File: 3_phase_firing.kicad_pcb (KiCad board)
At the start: 2 copper layers, 142.5 x 77.5 mm, 66 parts, among them J1 IN1, J2 IN2, J3 OUT, J4 USB_LED, J5 POWER, Q1 MMBT3904, Q2 MMBT3904, Q3 MMBT3904, U1 LM339, U10 4N35, U11 4N35, U12 4N35, U2 L7812, U3 4N35, U4 4N35, U5 4N35, U6 YAAJ_WeAct_BlackPill_Part_Like, U7 4N35, U8 4N35, U9 4N35

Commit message: fixing schematics and pcb layout, adding usb and knob control
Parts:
- removed G***: LOGO, logo_uny:logo_uny_15mm
- removed R28, R29: 220, Resistor_SMD:R_0805_2012Metric
- removed REF** (x3): MountingHole_3.2mm_M3_DIN965_Pad, MountingHole:MountingHole_3.2mm_M3_DIN965_Pad
- added J6: Conn_01x02, Connector_JST:JST_XH_B2B-XH-A_1x02_P2.50mm_Vertical, F.Cu at (167.6, 48.3)
- added J7: Conn_01x03, Connector_JST:JST_XH_B3B-XH-A_1x03_P2.50mm_Vertical, F.Cu at (132.1, 48.3)
- added J8: Conn_01x02, Connector_JST:JST_XH_B2B-XH-A_1x02_P2.50mm_Vertical, F.Cu at (157.5, 48.3)
- added Q4: MMBT3904, Package_TO_SOT_SMD:SOT-23, F.Cu at (162.6, 86.4)
- added Q5: MMBT3904, Package_TO_SOT_SMD:SOT-23, F.Cu at (164.2, 71.1)
- added Q6: MMBT3904, Package_TO_SOT_SMD:SOT-23, F.Cu at (162.6, 104.1)
- added kibuzzard-63D55C26: G***, kibuzzard-63D55C26, F.Cu at (77.9, 63.1)
- J4: value USB_LED -> USB_B; footprint Connector_JST:JST_XH_B2B-XH-A_1x02_P2.50mm_Vertical -> Connector_USB:USB_B_OST_USB-B1HSxx_Horizontal
- J5: value POWER -> Conn_01x03; footprint Connector_JST:JST_XH_B2B-XH-A_1x02_P2.50mm_Vertical -> Connector_JST:JST_XH_B3B-XH-A_1x03_P2.50mm_Vertical
- moved J3 114.8 mm to (128.3, 27.7), turned to 0 degrees
- moved J5 75.0 mm to (144.8, 48.3)
- moved D5 18.4 mm to (100.1, 68.1)
- moved C1 8.26 mm to (90.8, 59.6), turned to 180 degrees
- moved J4 4.77 mm to (167.6, 110.3), turned to -90 degrees
- moved R4 1.31 mm to (98.6, 93.4), turned to 90 degrees
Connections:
- net Net-(C1-Pad1) renamed /DB_D_OUT
- D1 pad 1: GNDS -> /DB_OUT
- D1 pad 2: PHASE_A -> GNDS
- D1 pad 3: Net-(D1-Pad3) -> NEUT
- D1 pad 4: NEUT -> PHASE_A
- D5 pad 2: Net-(D1-Pad3) -> /DB_OUT
- J4 pad 1: Net-(J4-Pad1) -> unconnected-(J4-Pad1)
- J4 pad 2: GND -> unconnected-(J4-Pad2)
- J5 pad 1: Net-(J5-Pad1) -> +3.3V
- J5 pad 2: GND -> ANGLE_CONTROL
- U6 pad 2: LED_USB -> LED_INDICATOR_2
- U6 pad 22: unconnected-(U6-Pad22) -> LED_INDICATOR_1
- U6 pad 26: ZCD_A -> ANGLE_CONTROL
- U6 pad 27: GATE_A1 -> unconnected-(U6-Pad27)
- U6 pad 28: GATE_A2 -> unconnected-(U6-Pad28)
- U6 pad 3: unconnected-(U6-Pad3) -> TRIAC_MODE
- U6 pad 31: unconnected-(U6-Pad31) -> ZCD_A
- U6 pad 4: TRIAC_MODE -> SCR_MODE
- U6 pad 7: unconnected-(U6-Pad7) -> GATE_A2
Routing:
- net TRIAC_MODE: track 110.2 -> 0.00 mm, vias 6 -> 0
- net ZCD_A: track 81.9 -> 0.00 mm, vias 2 -> 0
- net ZCD_B: track 79.7 -> 0.00 mm, vias 2 -> 0
- net LED_USB: track 74.1 -> 0.00 mm, vias 1 -> 0
- net GNDS: track 85.3 -> 16.1 mm, vias 22 -> 37
- net GATE_C1: track 54.0 -> 0.00 mm, vias 1 -> 0
- net GATE_C2: track 46.3 -> 0.00 mm
- net GATE_A1: track 35.2 -> 0.00 mm
- net PHASE_A: track 33.3 -> 0.00 mm
- net OUTC2_C: track 30.9 -> 0.00 mm, vias 1 -> 0
- net OUTB2_C: track 30.6 -> 0.00 mm, vias 1 -> 0
- net OUTA2_C: track 30.4 -> 0.00 mm, vias 1 -> 0
- net OUTC2_E: track 29.4 -> 0.00 mm
- net GATE_A2: track 28.7 -> 0.00 mm, vias 2 -> 0
- net OUTB2_E: track 25.2 -> 0.00 mm
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- added copper zone on F.Cu, net /DB_D_OUT
- added copper zone on F.Cu, net /DB_OUT
- added copper zone on F.Cu, net GNDS
- added copper zone on F.Cu, net NEUT
- added copper zone on F.Cu, net Net-(R5-Pad1)
- added copper zone on F.Cu, net PHASE_A
- added copper zone on F.Cu, net PHASE_B
- added copper zone on F.Cu, net PHASE_C
- added copper zone on B.Cu, net VCC
- removed copper zone on F.Cu, net +3.3V
- removed copper zone on B.Cu, net GND
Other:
- board text added: "HW-ID : ACRC-01 REV NUM : v0.3"
- board text removed: "!!!HIGH VOLTAGE!!!"
- board text removed: "HW-ID : ACRC-01 REV NUM : v0.2"
- board text removed: "N"

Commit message: done with all revision
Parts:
- removed D11: 1N4007, Diode_SMD:D_SMA_Handsoldering
- removed Q4, Q5, Q6: MMBT3904, Package_TO_SOT_SMD:SOT-23
- added R28: 1K, Resistor_SMD:R_1206_3216Metric_Pad1.30x1.75mm_HandSolder, F.Cu at (186.6, 69.1)
- added R29: 1K, Resistor_SMD:R_1206_3216Metric_Pad1.30x1.75mm_HandSolder, F.Cu at (186.6, 66.6)
- added R30: 1K, Resistor_SMD:R_1206_3216Metric_Pad1.30x1.75mm_HandSolder, B.Cu at (186.6, 69.1)
- added R31: 1K, Resistor_SMD:R_1206_3216Metric_Pad1.30x1.75mm_HandSolder, B.Cu at (186.6, 66.6)
- added R32: 1K, Resistor_SMD:R_1206_3216Metric_Pad1.30x1.75mm_HandSolder, F.Cu at (186.6, 83.7)
- added R33: 1K, Resistor_SMD:R_1206_3216Metric_Pad1.30x1.75mm_HandSolder, F.Cu at (186.6, 86.2)
- added R34: 1K, Resistor_SMD:R_1206_3216Metric_Pad1.30x1.75mm_HandSolder, B.Cu at (186.6, 83.7)
- added R35: 1K, Resistor_SMD:R_1206_3216Metric_Pad1.30x1.75mm_HandSolder, B.Cu at (186.6, 86.2)
- added R36: 1K, Resistor_SMD:R_1206_3216Metric_Pad1.30x1.75mm_HandSolder, F.Cu at (186.6, 100.9)
- added R37: 1K, Resistor_SMD:R_1206_3216Metric_Pad1.30x1.75mm_HandSolder, F.Cu at (186.6, 103.4)
- added R38: 1K, Resistor_SMD:R_1206_3216Metric_Pad1.30x1.75mm_HandSolder, B.Cu at (186.6, 100.9)
- added R39: 1K, Resistor_SMD:R_1206_3216Metric_Pad1.30x1.75mm_HandSolder, B.Cu at (186.6, 103.4)
- added R40: 220, Resistor_SMD:R_1206_3216Metric_Pad1.30x1.75mm_HandSolder, F.Cu at (132.1, 55.4)
- added R41: 10K, Resistor_SMD:R_0805_2012Metric, F.Cu at (168.8, 55.5)
- added R42: 10K, Resistor_SMD:R_0805_2012Metric, F.Cu at (153.0, 52.8)
- added REF**: MountingHole_3.2mm_M3, MountingHole:MountingHole_3.2mm_M3, F.Cu at (177.5, 116.2)
- added REF**: MountingHole_3.2mm_M3, MountingHole:MountingHole_3.2mm_M3, F.Cu at (80.1, 54.8)
- added REF**: MountingHole_3.2mm_M3, MountingHole:MountingHole_3.2mm_M3, F.Cu at (152.6, 116.2)
- added REF**: MountingHole_3.2mm_M3, MountingHole:MountingHole_3.2mm_M3, F.Cu at (200.1, 46.5)
- added REF**: MountingHole_3.2mm_M3, MountingHole:MountingHole_3.2mm_M3, F.Cu at (110.1, 101.8)
- added REF**: MountingHole_3.2mm_M3, MountingHole:MountingHole_3.2mm_M3, F.Cu at (200.1, 115.8)
- added kibuzzard-63D8BD9F: G***, kibuzzard-63D8BD9F, F.Cu at (154.6, 111.7)
- added kibuzzard-63DA9566: G***, kibuzzard-63DA9566, F.Cu at (207.2, 58.4)
- added kibuzzard-63DA9566: G***, kibuzzard-63DA9566, F.Cu at (207.1, 99.1)
- added kibuzzard-63DA95C1: G***, kibuzzard-63DA95C1, F.Cu at (192.6, 68.5)
- added kibuzzard-63DA9616: G***, kibuzzard-63DA9616, F.Cu at (192.6, 109.5)
- added kibuzzard-63DA961C: G***, kibuzzard-63DA961C, F.Cu at (192.6, 89.2)
- added kibuzzard-63DA96B7: G***, kibuzzard-63DA96B7, F.Cu at (207.2, 68.6)
- added kibuzzard-63DA96B7: G***, kibuzzard-63DA96B7, F.Cu at (207.1, 109.2)
- added kibuzzard-63DA974B: G***, kibuzzard-63DA974B, F.Cu at (207.2, 63.5)
- added kibuzzard-63DA974B: G***, kibuzzard-63DA974B, F.Cu at (207.1, 104.2)
- added kibuzzard-63DA9751: G***, kibuzzard-63DA9751, F.Cu at (207.2, 53.5)
- added kibuzzard-63DA9751: G***, kibuzzard-63DA9751, F.Cu at (207.1, 94.2)
- added kibuzzard-63DA9A23: G***, kibuzzard-63DA9A23, F.Cu at (170.9, 45.0)
- added kibuzzard-63DA9A91: G***, kibuzzard-63DA9A91, F.Cu at (158.7, 45.0)
- added kibuzzard-63DA9AA3: G***, kibuzzard-63DA9AA3, F.Cu at (145.7, 45.0)
- added kibuzzard-63DA9AAF: G***, kibuzzard-63DA9AAF, F.Cu at (130.5, 45.0)
- D10, D8: moved to B.Cu
- D7: moved to F.Cu
- J1, J2: footprint TerminalBlock:TerminalBlock_bornier-2_P5.08mm -> TerminalBlock_Phoenix:TerminalBlock_Phoenix_MKDS-1,5-2-5.08_1x02_P5.08mm_Horizontal
- J3: value OUT -> OUTPUT; footprint TerminalBlock_Phoenix:TerminalBlock_Phoenix_MKDS-3-12-5.08_1x12_P5.08mm_Horizontal -> TerminalBlock_Phoenix:TerminalBlock_Phoenix_MKDS-1,5-12-5.08_1x12_P5.08mm_Horizontal
- J5: value Conn_01x03 -> KNOB_ANGLE
- J6: value Conn_01x02 -> TRIAC_BUTTON_CONN
- J7: value Conn_01x03 -> LED_CONN
- J8: value Conn_01x02 -> SCR_BUTTON_CONN
- R22, R24, R26: value 2K2 -> 220
- R23, R25, R27: value 2K2 -> 220; moved to F.Cu
- U10, U11, U12, U7, U8, U9: value 4N35 -> MOC3021M
- U6: value YAAJ_WeAct_BlackPill_Part_Like -> STM32F401CCU6
- moved J3 109.0 mm to (200.6, 109.2), turned to 90 degrees
- moved D5 88.5 mm to (188.3, 61.4), turned to 0 degrees
- moved D7 25.9 mm to (188.3, 95.6), turned to 0 degrees
- moved D9 25.7 mm to (188.3, 78.5), turned to 0 degrees
- moved R25 23.9 mm to (166.4, 86.4)
- moved U10 22.4 mm to (175.2, 81.2)
- moved U9 22.4 mm to (175.2, 81.2)
- moved D10 22.0 mm to (188.3, 95.6), turned to 0 degrees
- moved D6 21.9 mm to (188.3, 78.5), turned to 0 degrees
- moved D8 21.8 mm to (188.3, 61.4), turned to 0 degrees
- moved Q2 19.5 mm to (162.9, 82.9)
- moved U7 18.6 mm to (175.2, 64.0)
- moved U8 18.5 mm to (175.2, 64.0)
- moved Q1 17.6 mm to (162.9, 65.8)
- moved R23 15.5 mm to (166.4, 69.2)
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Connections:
- D1 pad 1: /DB_OUT -> /DB_D_OUT
- D10 pad 2: GATE_C1 -> LOAD_C
- D5 pad 1: /DB_D_OUT -> Net-(D5-Pad1)
- D5 pad 2: /DB_OUT -> A
- D6 pad 2: GATE_B1 -> B
- D7 pad 2: GATE_B2 -> C
- D8 pad 2: GATE_A1 -> LOAD_A
- D9 pad 2: GATE_A2 -> LOAD_B
- J3 pad 1: OUTC2_E -> C
- J3 pad 10: OUTA2_C -> SCR_G2_A
- J3 pad 11: OUTA1_E -> SCR_G1_A
- J3 pad 12: OUTA1_C -> LOAD_A
- J3 pad 2: OUTC2_C -> SCR_G2_C
- J3 pad 3: OUTC1_E -> SCR_G1_C
- J3 pad 4: OUTC1_C -> LOAD_C
- J3 pad 5: OUTB2_E -> B
- J3 pad 6: OUTB2_C -> SCR_G2_B
- J3 pad 7: OUTB1_E -> SCR_G1_B
- J3 pad 8: OUTB1_C -> LOAD_B
- J3 pad 9: OUTA2_E -> A
- J4 pad 1: unconnected-(J4-Pad1) -> +5V
- J4 pad 2: unconnected-(J4-Pad2) -> USB-
- J4 pad 3: unconnected-(J4-Pad3) -> USB+
- J4 pad 4: unconnected-(J4-Pad4) -> GND
- J7 pad 2: LED_INDICATOR_1 -> Net-(J7-Pad2)
- Q1 pad 1: TRIAC_MODE -> MODE_SELECT
- Q1 pad 2: Net-(D7-Pad1) -> GATE_A2
- Q1 pad 3: Net-(D6-Pad1) -> GATE_A1
- Q2 pad 1: TRIAC_MODE -> MODE_SELECT
- Q2 pad 2: Net-(D9-Pad1) -> GATE_B2
- Q2 pad 3: Net-(D8-Pad1) -> GATE_B1
- Q3 pad 1: TRIAC_MODE -> MODE_SELECT
- Q3 pad 2: Net-(D11-Pad1) -> GATE_C2
- Q3 pad 3: Net-(D10-Pad1) -> GATE_C1
- R22 pad 2: Net-(D6-Pad1) -> GATE_B1
- R23 pad 2: Net-(D7-Pad1) -> GATE_A2
- R24 pad 2: Net-(D8-Pad1) -> GATE_A1
- R25 pad 2: Net-(D9-Pad1) -> GATE_B2
- R26 pad 2: Net-(D10-Pad1) -> GATE_C1
- R27 pad 2: Net-(D11-Pad1) -> GATE_C2
- U10 pad 4: OUTA2_E -> Net-(D9-Pad1)
- U10 pad 5: OUTA2_C -> unconnected-(U10-Pad5)
- U10 pad 6: unconnected-(U10-Pad6) -> Net-(R34-Pad2)
- U11 pad 4: OUTC1_E -> Net-(R36-Pad2)
- U11 pad 5: OUTC1_C -> unconnected-(U11-Pad5)
- U11 pad 6: unconnected-(U11-Pad6) -> Net-(D7-Pad1)
- U12 pad 4: OUTC2_E -> Net-(D10-Pad1)
- U12 pad 5: OUTC2_C -> unconnected-(U12-Pad5)
- U12 pad 6: unconnected-(U12-Pad6) -> Net-(R38-Pad2)
- U6 pad 37: unconnected-(U6-Pad37) -> GATE_A2
- U6 pad 40: unconnected-(U6-Pad40) -> +5V
- U6 pad 7: GATE_A2 -> MODE_SELECT
- U6 pad 8: unconnected-(U6-Pad8) -> USB+
- U6 pad 9: unconnected-(U6-Pad9) -> USB-
- U7 pad 1: Net-(R22-Pad1) -> Net-(R24-Pad1)
- U7 pad 4: OUTB1_E -> Net-(R28-Pad2)
- U7 pad 5: OUTB1_C -> unconnected-(U7-Pad5)
- U7 pad 6: unconnected-(U7-Pad6) -> Net-(D5-Pad1)
- U8 pad 4: OUTB2_E -> Net-(D8-Pad1)
- U8 pad 5: OUTB2_C -> unconnected-(U8-Pad5)
- U8 pad 6: unconnected-(U8-Pad6) -> Net-(R30-Pad2)
- U9 pad 1: Net-(R24-Pad1) -> Net-(R22-Pad1)
- U9 pad 4: OUTA1_E -> Net-(R32-Pad2)
- U9 pad 5: OUTA1_C -> unconnected-(U9-Pad5)
- U9 pad 6: unconnected-(U9-Pad6) -> Net-(D6-Pad1)
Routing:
- net ZCD_A: track 0.00 -> 98.5 mm
- net ZCD_B: track 0.00 -> 87.9 mm, vias 0 -> 1
- net MODE_SELECT: track 0.00 -> 83.2 mm, vias 0 -> 5
- net USB+: track 0.00 -> 68.0 mm, vias 0 -> 2
- net USB-: track 0.00 -> 64.4 mm, vias 0 -> 2
- net LED_INDICATOR_1: track 0.00 -> 62.6 mm, vias 0 -> 1
- net GATE_C1: track 0.00 -> 62.5 mm, vias 0 -> 2
- net +5V: track 0.00 -> 60.8 mm
- net GATE_C2: track 0.00 -> 53.5 mm, vias 0 -> 1
- net ANGLE_CONTROL: track 0.00 -> 51.1 mm, vias 0 -> 1
- net TRIAC_MODE: track 0.00 -> 39.2 mm, vias 0 -> 1
- net SCR_G2_C: track 0.00 -> 32.7 mm
- net SCR_MODE: track 0.00 -> 29.9 mm, vias 0 -> 2
- net SCR_G2_A: track 0.00 -> 29.0 mm
- net SCR_G2_B: track 0.00 -> 28.7 mm
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- added copper zone on F.Cu, net +3.3V
- added copper zone on F.Cu, net A
- added copper zone on F.Cu, net B
- added copper zone on F.Cu, net C
- added copper zone on B.Cu, net GND
- added copper zone on B.Cu, net SCR_G1_A
- added copper zone on F.Cu, net SCR_G1_A
- added copper zone on B.Cu, net SCR_G1_B
- added copper zone on F.Cu, net SCR_G1_B
- added copper zone on B.Cu, net SCR_G1_C
- added copper zone on F.Cu, net SCR_G1_C
- removed copper zone on F.Cu, net /DB_OUT
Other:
- board size 142.5 x 77.5 mm -> 136.7 x 77.5 mm
- board text added: "A1"
- board text added: "A2"
- board text added: "G1"
- board text added: "G2"
- board text removed: "DESIGN : HILAL YAHYA SUPERVISOR :"

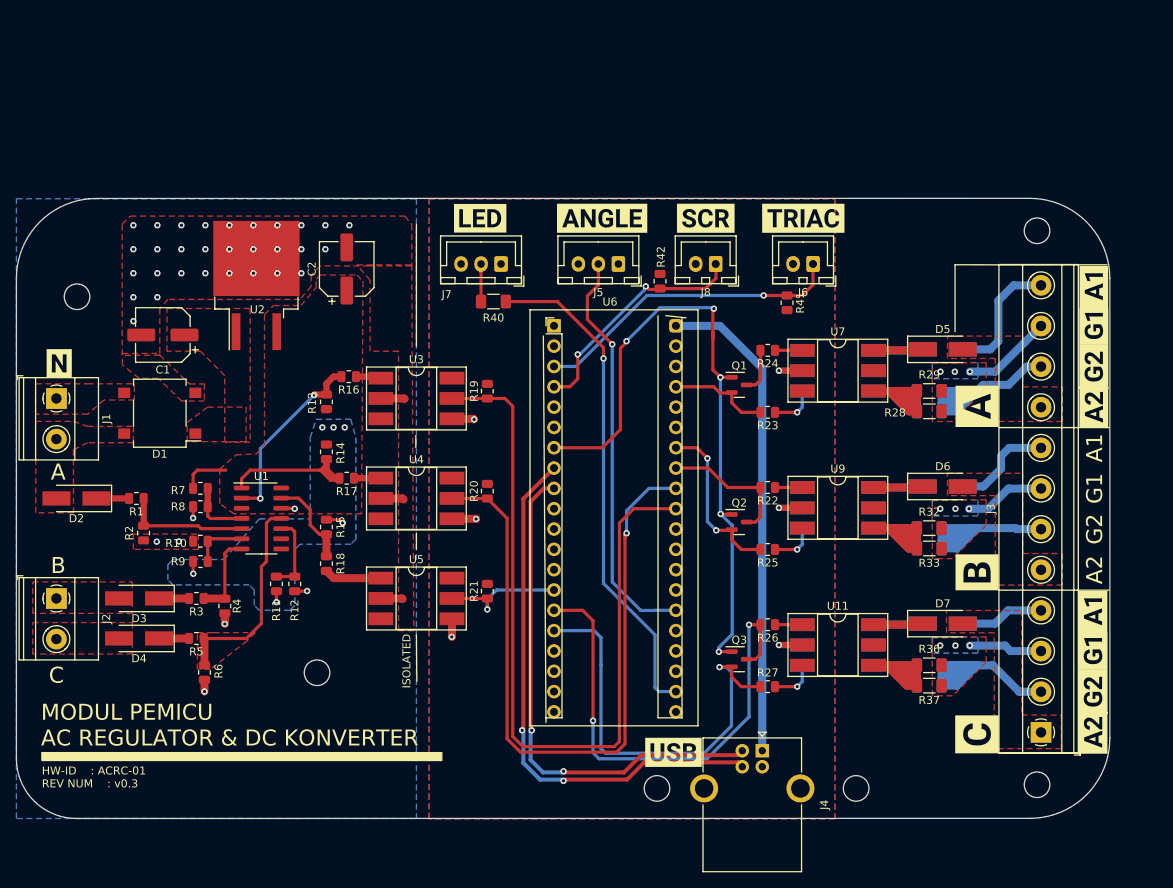
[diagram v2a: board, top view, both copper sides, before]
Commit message: fixing psu issue and 3d libs update
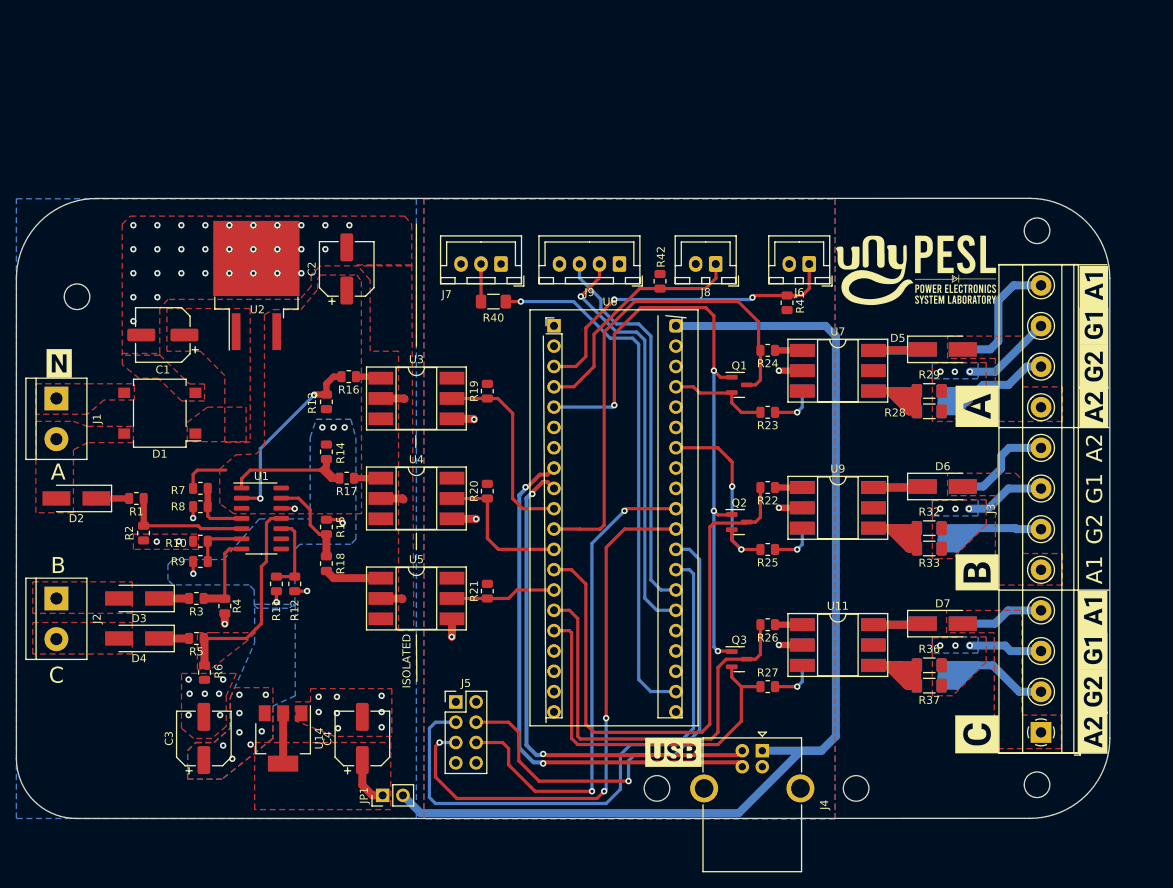
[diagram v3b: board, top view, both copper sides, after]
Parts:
- removed the REF** at (110.1, 101.8)
- removed kibuzzard-63DA9A23: G***, kibuzzard-63DA9A23
- removed kibuzzard-63DA9A91: G***, kibuzzard-63DA9A91
- removed kibuzzard-63DA9AA3: G***, kibuzzard-63DA9AA3
- removed kibuzzard-63DA9AAF: G***, kibuzzard-63DA9AAF
- added C3: 10uF, Capacitor_SMD:CP_Elec_6.3x7.7, F.Cu at (95.9, 110.0)
- added C4: 10uF, Capacitor_SMD:CP_Elec_6.3x7.7, F.Cu at (115.7, 110.0)
- added G***: LOGO, logo_uny:logo-unypels, F.Cu at (185.0, 51.5)
- added J9: Conn_01x04, Connector_JST:JST_XH_B4B-XH-A_1x04_P2.50mm_Vertical, F.Cu at (147.9, 50.7)
- added JP1: Jumper_2_Open, Connector_PinHeader_2.54mm:PinHeader_1x02_P2.54mm_Vertical, F.Cu at (118.3, 117.1)
- added U14: AMS1117-5.0, Package_TO_SOT_SMD:SOT-223-3_TabPin2, F.Cu at (105.8, 110.0)
- J1, J2: footprint TerminalBlock_Phoenix:TerminalBlock_Phoenix_MKDS-1,5-2-5.08_1x02_P5.08mm_Horizontal -> TerminalBlock:TerminalBlock_bornier-2_P5.08mm
- J5: value KNOB_ANGLE -> Conn_02x04_Counter_Clockwise; footprint Connector_JST:JST_XH_B3B-XH-A_1x03_P2.50mm_Vertical -> Connector_PinHeader_2.54mm:PinHeader_2x04_P2.54mm_Vertical
- moved J5 58.4 mm to (127.4, 105.4), turned to 0 degrees
- moved J6 0.48 mm to (171.6, 50.7)
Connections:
- J5 pad 2: ANGLE_CONTROL -> GND
- J5 pad 3: GND -> AUX_ADC1
- U6 pad 10: unconnected-(U6-Pad10) -> ZCD_A
- U6 pad 11: unconnected-(U6-Pad11) -> GATE_A1
- U6 pad 12: unconnected-(U6-Pad12) -> ZCD_B
- U6 pad 13: unconnected-(U6-Pad13) -> GATE_B1
- U6 pad 26: ANGLE_CONTROL -> ANG_CNTR_A
- U6 pad 27: unconnected-(U6-Pad27) -> ANG_CNTR_B
- U6 pad 28: unconnected-(U6-Pad28) -> AUX_ADC1
- U6 pad 29: unconnected-(U6-Pad29) -> AUX_ADC2
- U6 pad 30: unconnected-(U6-Pad30) -> AUX_ADC3
- U6 pad 31: ZCD_A -> AUX_ADC4
- U6 pad 32: ZCD_B -> AUX_ADC5
- U6 pad 33: GATE_B1 -> AUX_ADC6
- U6 pad 5: unconnected-(U6-Pad5) -> MODE_SELECT
- U6 pad 7: MODE_SELECT -> unconnected-(U6-PA10-Pad7)
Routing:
- net +5V: track 60.8 -> 137.0 mm
- net ZCD_A: track 98.5 -> 24.7 mm
- net AUX_ADC1: track 0.00 -> 73.7 mm
- net ZCD_B: track 87.9 -> 18.3 mm, vias 1 -> 0
- net AUX_ADC3: track 0.00 -> 69.1 mm, vias 0 -> 3
- net AUX_ADC2: track 0.00 -> 62.0 mm, vias 0 -> 1
- net AUX_ADC4: track 0.00 -> 61.5 mm, vias 0 -> 2
- net GATE_B1: track 17.2 -> 73.8 mm
- net GATE_A1: track 5.67 -> 61.9 mm
- net ANG_CNTR_A: track 0.00 -> 52.1 mm, vias 0 -> 1
- net ANGLE_CONTROL: track 51.1 -> 0.00 mm, vias 1 -> 0
- net ANG_CNTR_B: track 0.00 -> 48.5 mm
- net Net-(JP1-A): track 0.00 -> 12.5 mm
- net GATE_C1: track 62.5 -> 53.9 mm, vias 2 -> 0
- net GATE_C2: track 53.5 -> 47.9 mm, vias 1 -> 0
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- added copper zone on F.Cu, net Net-(JP1-A)
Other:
- board text removed: "HW-ID : ACRC-01 REV NUM : v0.3"
- board text removed: "MODUL PEMICU AC REGULATOR & DC KONVERTER"

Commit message: fixing unconnected bootstrap
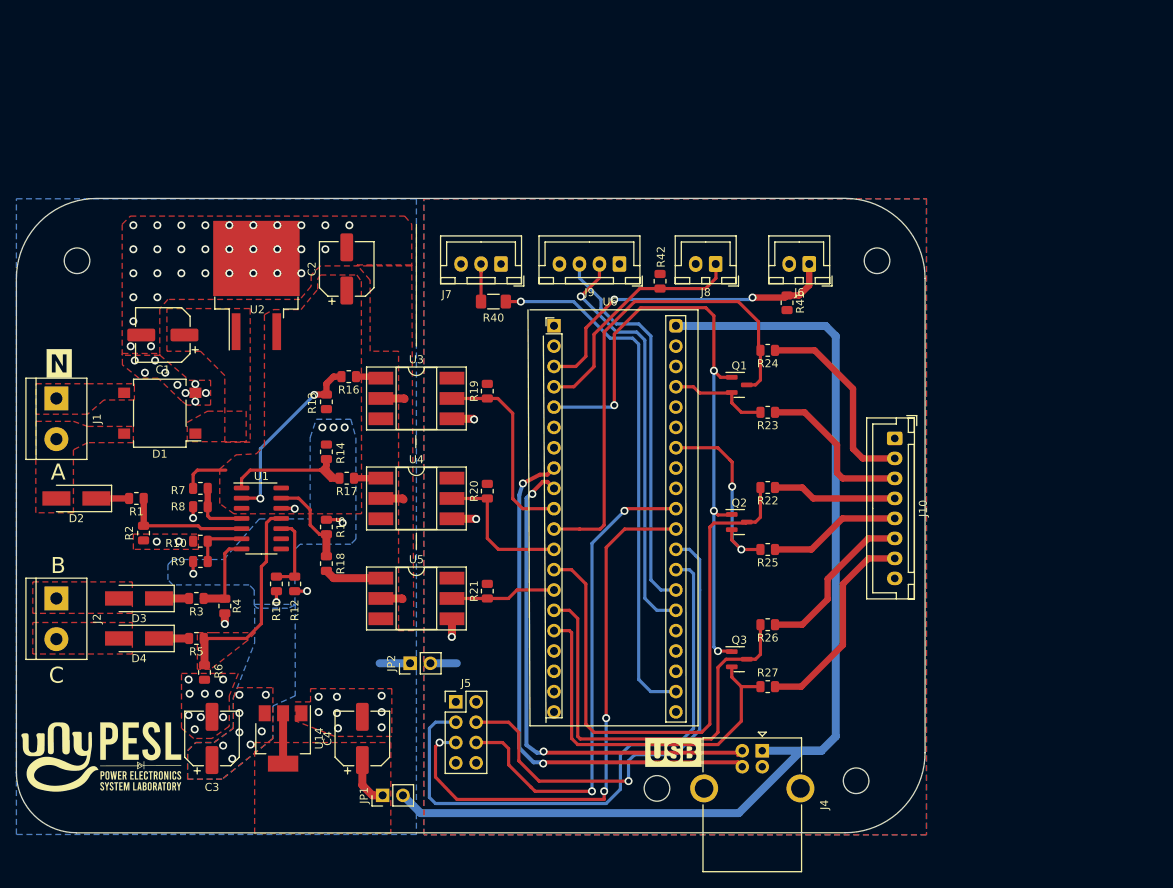
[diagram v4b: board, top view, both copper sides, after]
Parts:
- removed D10, D5, D6, D7, D8, D9: 1N4007, Diode_SMD:D_SMA_Handsoldering
- removed J3: OUTPUT, TerminalBlock_Phoenix:TerminalBlock_Phoenix_MKDS-1,5-12-5.08_1x12_P5.08mm_Horizontal
- removed R28, R29, R30, R31, R32, R33, R34, R35, R36, R37, R38, R39: 1K, Resistor_SMD:R_1206_3216Metric_Pad1.30x1.75mm_HandSolder
- removed the REF** at (200.1, 115.8)
- removed U10, U11, U12, U7, U8, U9: MOC3021M, Package_DIP:DIP-6_W8.89mm_SMDSocket_LongPads
- removed kibuzzard-63DA9566 (x2): G***, kibuzzard-63DA9566
- removed kibuzzard-63DA95C1: G***, kibuzzard-63DA95C1
- removed kibuzzard-63DA9616: G***, kibuzzard-63DA9616
- removed kibuzzard-63DA961C: G***, kibuzzard-63DA961C
- removed kibuzzard-63DA96B7 (x2): G***, kibuzzard-63DA96B7
- removed kibuzzard-63DA974B (x2): G***, kibuzzard-63DA974B
- removed kibuzzard-63DA9751 (x2): G***, kibuzzard-63DA9751
- added J10: Conn_01x08, Connector_JST:JST_XH_B8B-XH-A_1x08_P2.50mm_Vertical, F.Cu at (182.3, 72.5)
- added JP2: Jumper_2_Open, Connector_PinHeader_2.54mm:PinHeader_1x02_P2.54mm_Vertical, F.Cu at (121.7, 100.6)
- moved G*** 118.6 mm to (83.1, 112.3)
- moved REF** 20.3 mm to (180.1, 50.3)
- moved REF** 4.50 mm to (80.1, 50.3)
- moved C3 1.02 mm to (96.9, 110.0)
- moved REF** 0.96 mm to (177.5, 115.3)
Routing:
- net SCR_G2_C: track 32.7 -> 0.00 mm
- net SCR_G2_A: track 29.0 -> 0.00 mm
- net SCR_G2_B: track 28.7 -> 0.00 mm
- net Net-(J10-Pin_2): track 3.41 -> 25.0 mm
- net Net-(J10-Pin_7): track 5.70 -> 26.1 mm, vias 1 -> 0
- net Net-(R36-Pad2): track 18.7 -> 0.00 mm
- net Net-(R28-Pad2): track 18.7 -> 0.00 mm
- net Net-(R32-Pad2): track 18.5 -> 0.00 mm
- net Net-(J10-Pin_6): track 3.41 -> 20.9 mm
- net Net-(R30-Pad2): track 17.5 -> 0.00 mm
- net Net-(R34-Pad2): track 17.4 -> 0.00 mm
- net Net-(R38-Pad2): track 17.4 -> 0.00 mm
- net LOAD_A: track 16.1 -> 0.00 mm
- net Net-(J10-Pin_3): track 5.70 -> 20.4 mm, vias 1 -> 0
- net LOAD_B: track 12.7 -> 0.00 mm
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- removed copper zone on F.Cu, net A
- removed copper zone on F.Cu, net B
- removed copper zone on F.Cu, net C
- removed copper zone on B.Cu, net SCR_G1_A
- removed copper zone on F.Cu, net SCR_G1_A
- removed copper zone on B.Cu, net SCR_G1_B
- removed copper zone on F.Cu, net SCR_G1_B
- removed copper zone on B.Cu, net SCR_G1_C
- removed copper zone on F.Cu, net SCR_G1_C
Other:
- board size 136.7 x 77.5 mm -> 113.6 x 79.3 mm
- board text removed: "A1"
- board text removed: "A2"
- board text removed: "G1"
- board text removed: "G2"
- board text removed: "ISOLATED"
